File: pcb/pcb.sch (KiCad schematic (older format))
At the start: 0 parts

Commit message: pcb: working on sch
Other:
- note added: "0"
- note added: "1"
- note added: "2"
- note added: "3"
- note added: "4"
- note added: "5"
- note added: "6"
- note added: "7"
- note added: "8"
- note added: "Audio Output\n"
- note added: "Clock & Debugging"
- note added: "Keypad"
- note added: "LPDDR2 Memory"
- note added: "Power Supply"
- note added: "SPI Flash & TF-Card"
- note added: "STN LCD"
- note added: "Table of Contents"
- note added: "USB"
- note added: "Unused IO"
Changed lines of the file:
@@
 $Descr A4 11693 8268
 encoding utf-8
-Sheet 1 7
+Sheet 1 10
 Title "RhythmPocket"
 Date ""
@@
 $EndDescr
 $Sheet
-S 1600 1400 2900 200
+S 1600 2000 2900 200
 U 5D180A01
 F0 "cpu" 50
@@
 $EndSheet
 $Sheet
-S 7900 4750 2700 1450
+S 1600 1600 2900 200
 U 5D4C99F9
 F0 "power" 50
@@
 $EndSheet
 $Sheet
-S 1600 1800 2900 200
+S 1600 2400 2900 200
 U 5D5090CA
 F0 "ddr" 50
@@
 $EndSheet
 $Sheet
-S 1600 2600 2900 200
+S 1600 2800 2900 200
 U 5DB2122B
 F0 "storage" 50
@@
 $EndSheet
 $Sheet
-S 1600 2200 2900 200
+S 1600 3600 2900 200
 U 5DB51F59
 F0 "lcd" 50
 F1 "lcd.sch" 50
 $EndSheet
+Text Notes 1700 2150 0    100  ~ 0
+Clock & Debugging
+Text Notes 1700 2550 0    100  ~ 0
+LPDDR2 Memory
+Text Notes 1700 3750 0    100  ~ 0
+STN LCD
+Text Notes 1700 2950 0    100  ~ 0
+SPI Flash & TF-Card
+Text Notes 1700 1400 0    118  Italic 24
+Table of Contents
+Text Notes 1700 1750 0    100  ~ 0
+Power Supply
 $Sheet
-S 7000 3800 1200 600
-U 5DB91D11
-F0 "fuckkicad" 50
-F1 "fuckkicad.sch" 50
+S 1600 3200 2900 200
+U 5D438133
+F0 "audio" 50
+F1 "audio.sch" 50
 $EndSheet
+Text Notes 1700 3350 0    100  ~ 0
+Audio Output\n
+$Sheet
+S 1600 4400 2900 200
+U 5D438406
+F0 "keypad" 50
+F1 "keypad.sch" 50
+$EndSheet
+$Sheet
+S 1600 4800 2900 200
+U 5D438456
+F0 "unused" 50
+F1 "unused.sch" 50
+$EndSheet
+Text Notes 1700 4550 0    100  ~ 0
+Keypad
+Text Notes 1700 4950 0    100  ~ 0
+Unused IO
+$Sheet
+S 1600 4000 2900 200
+U 5D1A413B
+F0 "usb" 50
+F1 "usb.sch" 50
+$EndSheet
+Text Notes 1700 4150 0    100  ~ 0
+USB
+Text Notes 1300 2150 0    100  ~ 0
+1
+Text Notes 1300 2550 0    100  ~ 0
+2
+Text Notes 1300 2950 0    100  ~ 0
+3
+Text Notes 1300 3350 0    100  ~ 0
+4
+Text Notes 1300 3750 0    100  ~ 0
+5
+Text Notes 1300 4150 0    100  ~ 0
+6
+Text Notes 1300 4550 0    100  ~ 0
+7
+Text Notes 1300 1750 0    100  ~ 0
+0
+Text Notes 1300 4950 0    100  ~ 0
+8
 $EndSCHEMATC

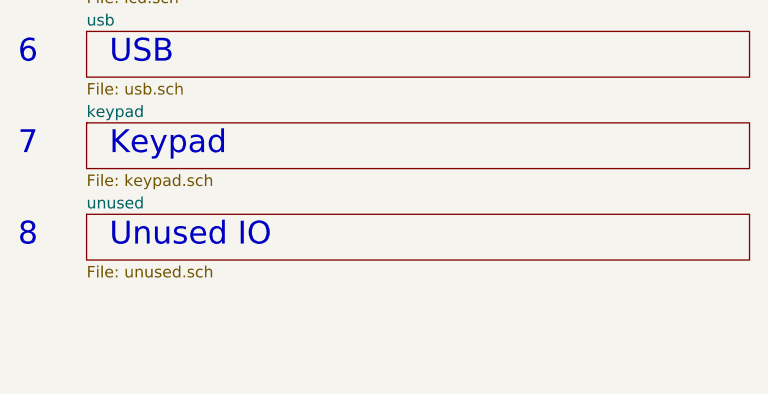
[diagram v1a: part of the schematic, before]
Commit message: pcb: draw sch for wifi & bt
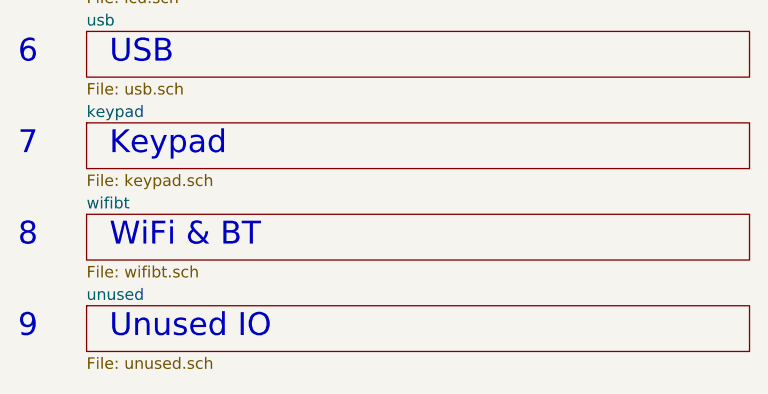
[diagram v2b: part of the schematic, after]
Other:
- note added: "9"
- note added: "WiFi & BT"
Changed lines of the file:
@@
 $Descr A4 11693 8268
 encoding utf-8
-Sheet 1 10
+Sheet 1 11
 Title "RhythmPocket"
 Date ""
@@
 $EndSheet
 $Sheet
-S 1600 4800 2900 200
+S 1600 5200 2900 200
 U 5D438456
 F0 "unused" 50
@@
 Text Notes 1700 4550 0    100  ~ 0
 Keypad
-Text Notes 1700 4950 0    100  ~ 0
+Text Notes 1700 5350 0    100  ~ 0
 Unused IO
 $Sheet
@@
 Text Notes 1300 1750 0    100  ~ 0
 0
+Text Notes 1300 5350 0    100  ~ 0
+9
+$Sheet
+S 1600 4800 2900 200
+U 5D1BA41C
+F0 "wifibt" 50
+F1 "wifibt.sch" 50
+$EndSheet
 Text Notes 1300 4950 0    100  ~ 0
 8
+Text Notes 1700 4950 0    100  ~ 0
+WiFi & BT
 $EndSCHEMATC

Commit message: pcb: finishing sch for r0.1
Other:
- note added: "Keypad & GPIO"
- note removed: "Keypad"
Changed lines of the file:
@@
 $EndSheet
 Text Notes 1700 4550 0    100  ~ 0
-Keypad
+Keypad & GPIO
 Text Notes 1700 5350 0    100  ~ 0
 Unused IO
